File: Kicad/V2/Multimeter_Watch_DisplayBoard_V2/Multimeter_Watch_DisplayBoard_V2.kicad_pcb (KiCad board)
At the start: 2 copper layers, 46 x 42 mm, 16 parts, among them J1 51281-1294, J2 Conn_01x11_Female, J3 Conn_01x11_Female, SW1 SW_Push, SW2 SW_Push, SW3 SW_Push, SW4 SW_Push, SW5 SW_Push, SW6 SW_Push

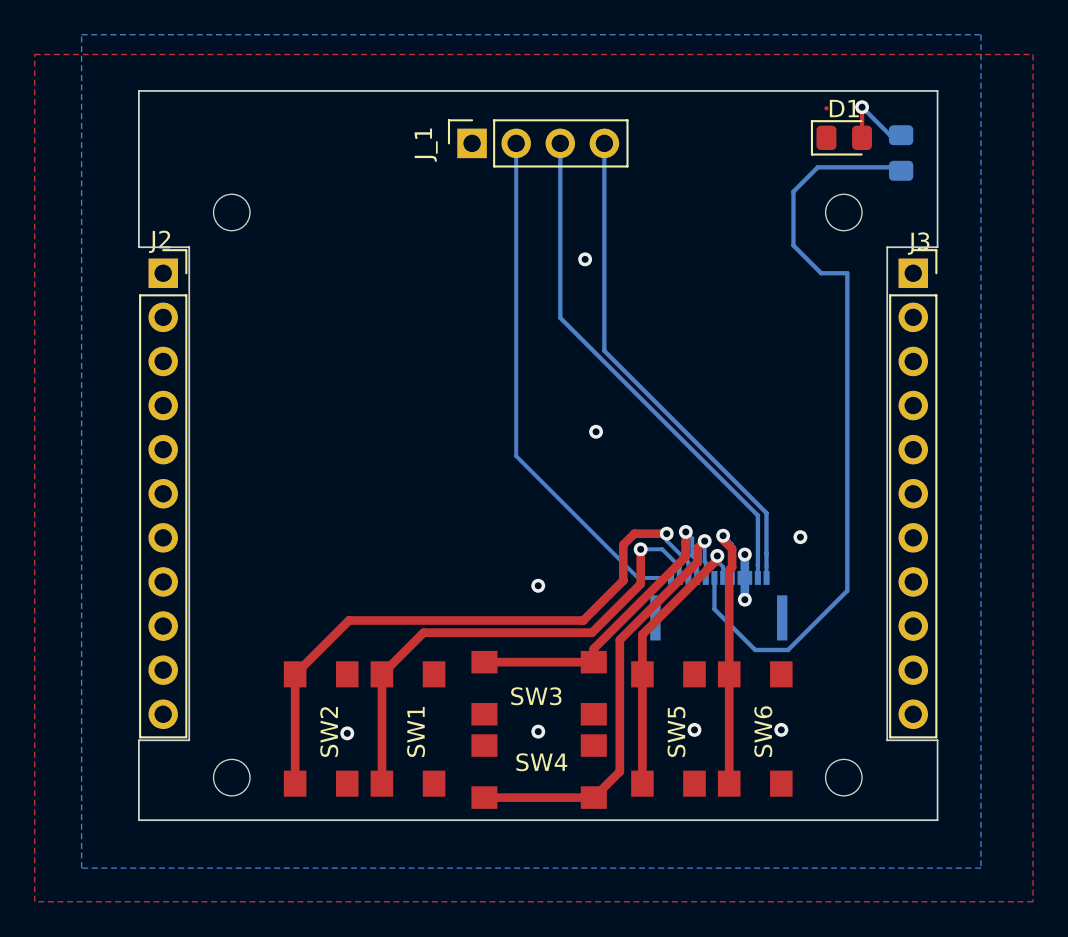
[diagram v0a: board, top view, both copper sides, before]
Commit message: V2 displayboard silkscreen improvements, move display measurements to separate layer
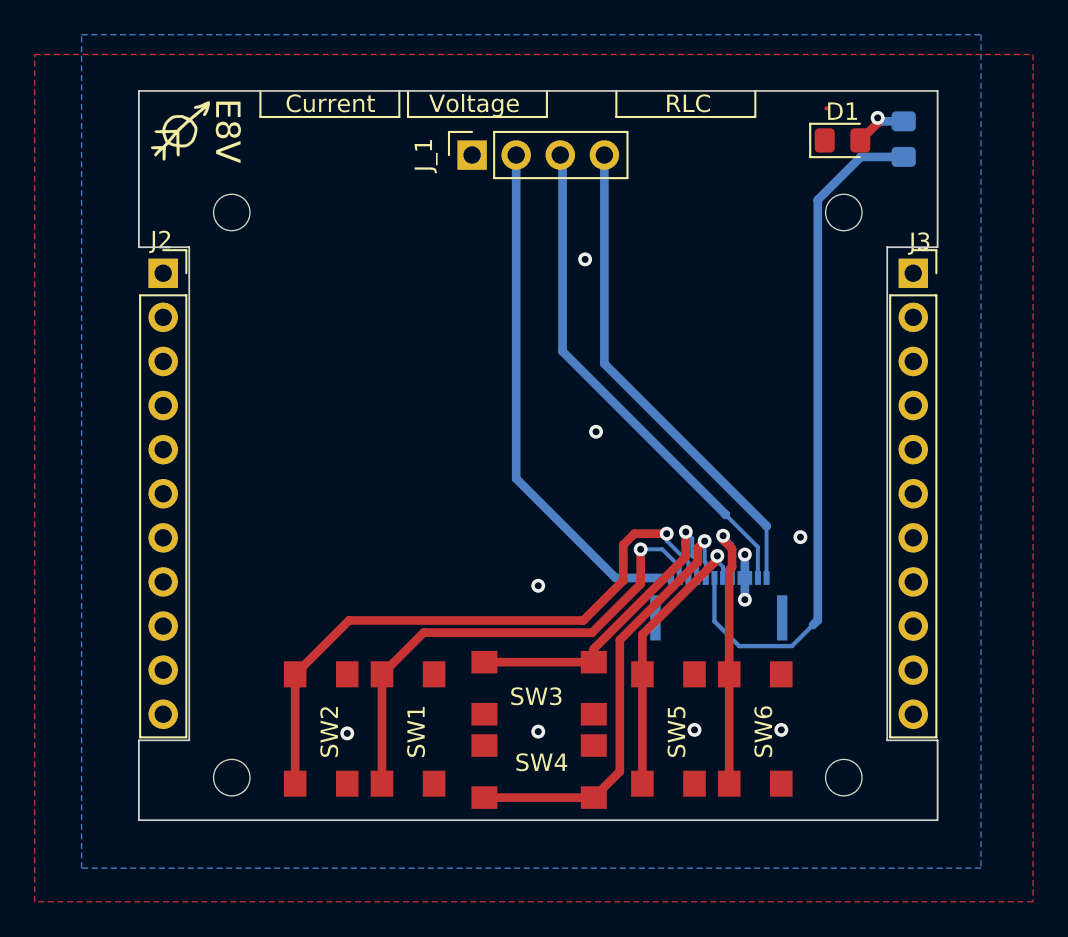
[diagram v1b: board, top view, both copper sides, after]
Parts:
- added G***: LOGO, Multimeter_Watch_Custom_Footprints:github_logo, B.Cu at (135.8, 74.5)
- added G***: LOGO, Multimeter_Watch_Custom_Footprints:nouth_signature3_4by3_4, F.Cu at (104.4, 60.3)
- moved R1 0.81 mm to (146.1, 60.8)
- moved J_1 0.67 mm to (121.2, 61.7)
- moved D1 0.18 mm to (142.5, 60.9)
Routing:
- net /PB5: track 43.8 -> 39.8 mm
- net Net-(D1-Pad2): track 4.68 -> 3.30 mm
- net /SCL: track 29.8 -> 29.1 mm
- net /SDA: track 28.9 -> 28.2 mm
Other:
- board text added: ":ptrbroz/Multimeter_watch"
- board text added: "Current"
- board text added: "E8V"
- board text added: "GND"
- board text added: "PB5"
- board text added: "PB6"
- board text added: "PB7"
- board text added: "PD3"
- board text added: "PD5"
- board text added: "PD6"
- board text added: "PE4"
- board text added: "PE5"
- board text added: "RLC"
- board text added: "SCL"
- board text added: "SDA"
- board text added: "Voltage"

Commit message: females layout improvements, add silkscreen labels for female pins
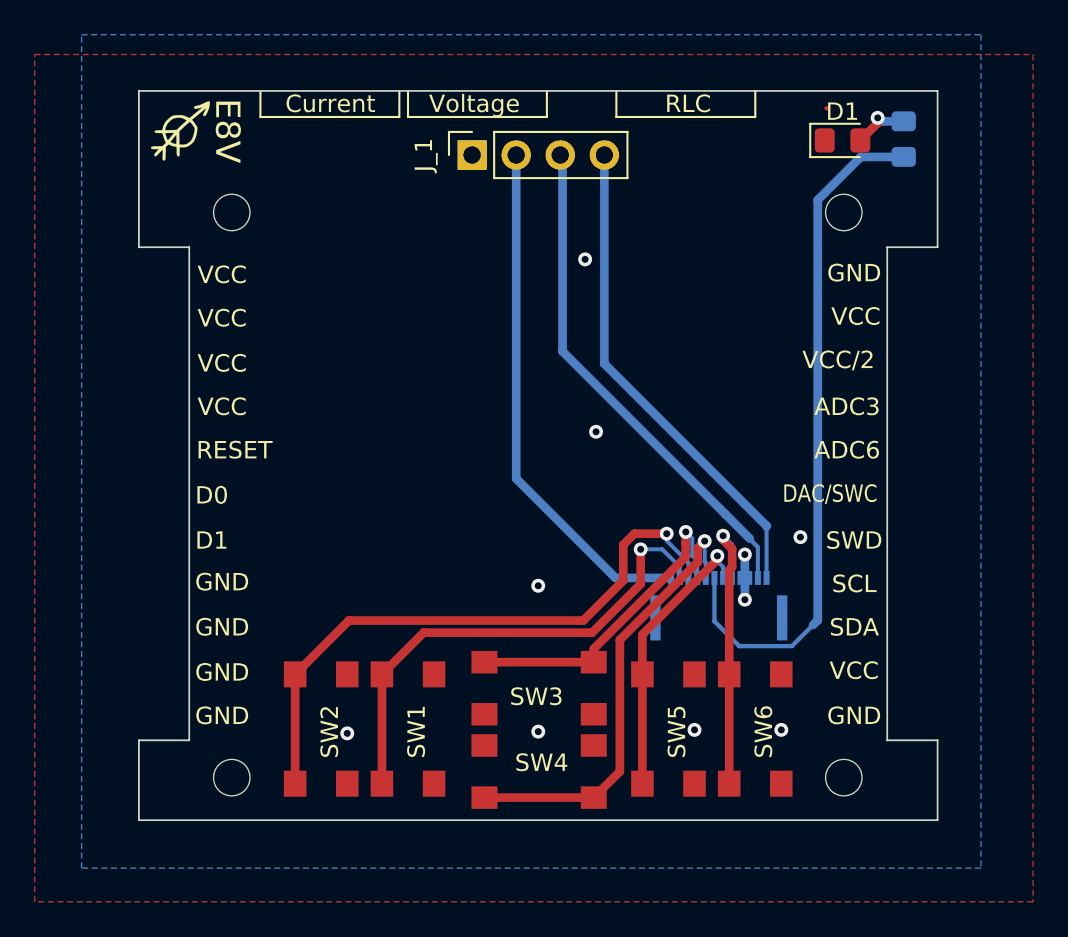
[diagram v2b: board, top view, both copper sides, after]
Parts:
- removed J2, J3: Conn_01x11_Female, Connector_PinSocket_2.54mm:PinSocket_1x11_P2.54mm_Vertical
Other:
- board text added: "ADC3"
- board text added: "ADC6"
- board text added: "D0"
- board text added: "D1"
- board text added: "DAC/SWC"
- board text added: "RESET"
- board text added: "SWD"
- board text added: "VCC"
- board text added: "VCC/2"

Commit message: top board rework (move flex conn up, dedicated display enable)
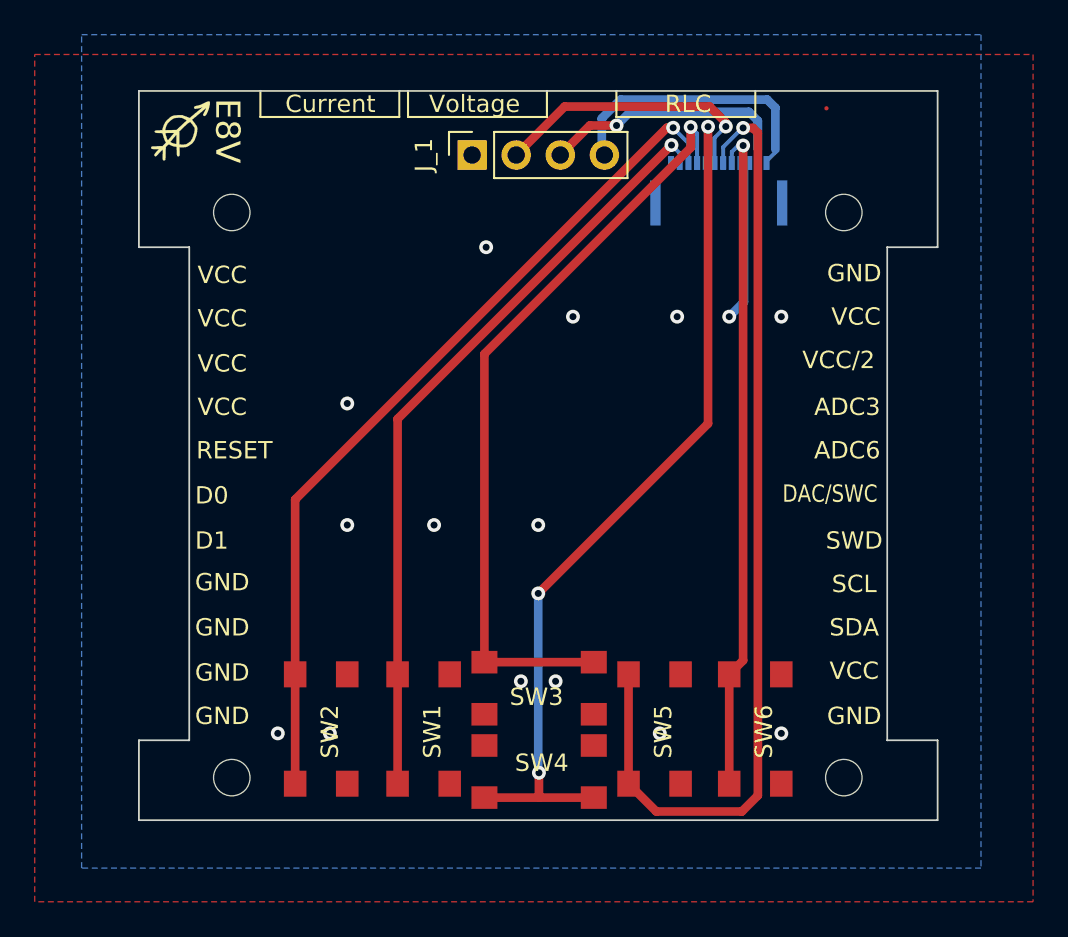
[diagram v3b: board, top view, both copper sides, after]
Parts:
- removed D1: LED, LED_SMD:LED_0805_2012Metric_Pad1.15x1.40mm_HandSolder
- removed R1: R, Resistor_SMD:R_0805_2012Metric_Pad1.15x1.40mm_HandSolder
- moved J1 23.9 mm to (135.4, 63.3)
- moved SW1 0.90 mm to (118.4, 94.8)
- moved SW5 0.80 mm to (131.7, 94.8)
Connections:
- J1 pad 1: /PD3 -> /VCC
- J_1 pad 2: /PD3 -> /PB5
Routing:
- net /PD5: track 16.3 -> 56.5 mm
- net /PD3: track 29.8 -> 0.00 mm
- net /PB6: track 18.9 -> 44.3 mm
- net /PB7: track 26.1 -> 51.2 mm, vias 1 -> 3
- net /PB5: track 39.8 -> 16.2 mm, vias 0 -> 1
- net /PD6: track 17.2 -> 38.5 mm
- net /PE4: track 28.7 -> 44.6 mm
- net /PE5: track 35.3 -> 49.4 mm
- net /SCL: track 29.1 -> 15.1 mm, vias 0 -> 1
- net /SDA: track 28.2 -> 16.2 mm
- net /GND: track 3.10 -> 9.70 mm, vias 10 -> 15
- net Net-(D1-Pad2): track 3.30 -> 0.00 mm, vias 1 -> 0
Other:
- board text removed: "PD3"

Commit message: make V2 displayboard use same pinout for buttons as V1
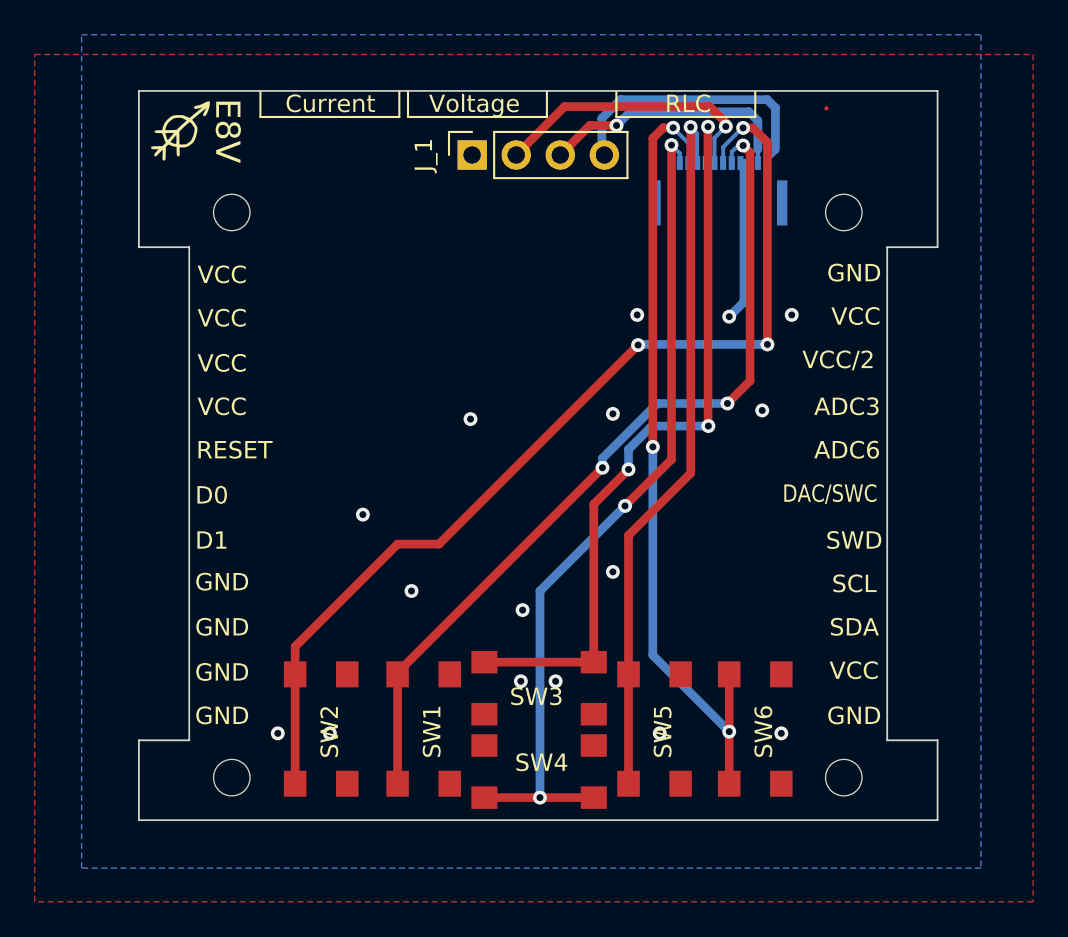
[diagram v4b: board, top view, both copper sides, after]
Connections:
- SW1 pad 1: /PE4 -> /PD6
- SW2 pad 1: /PE5 -> /PD5
- SW3 pad 1: /PB6 -> /PB7
- SW4 pad 1: /PB7 -> /PE4
- SW5 pad 1: /PD5 -> /PB6
- SW6 pad 1: /PD6 -> /PE5
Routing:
- net /PD6: track 38.5 -> 49.1 mm, vias 1 -> 3
- net /PB7: track 51.2 -> 43.9 mm
- net /PE4: track 44.6 -> 48.3 mm, vias 1 -> 3
- net /PE5: track 49.4 -> 46.1 mm, vias 1 -> 3
- net /PB6: track 44.3 -> 41.5 mm
- net /PD5: track 56.5 -> 58.2 mm, vias 1 -> 3
- net /GND: vias 15 -> 16

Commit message: add github to front silkscreen
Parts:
- added G***: LOGO, Multimeter_Watch_Custom_Footprints:github_logo_smaller, F.Cu at (143.3, 59.5)
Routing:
- net /GND: vias 16 -> 15
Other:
- board text added: "ptrbroz/Multimeter_watch"
